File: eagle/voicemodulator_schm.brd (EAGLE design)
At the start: 109 x 84 mm, 36 parts, among them T1 2N5089, T2 2N5089, T3 2N5089, T4 2N5089

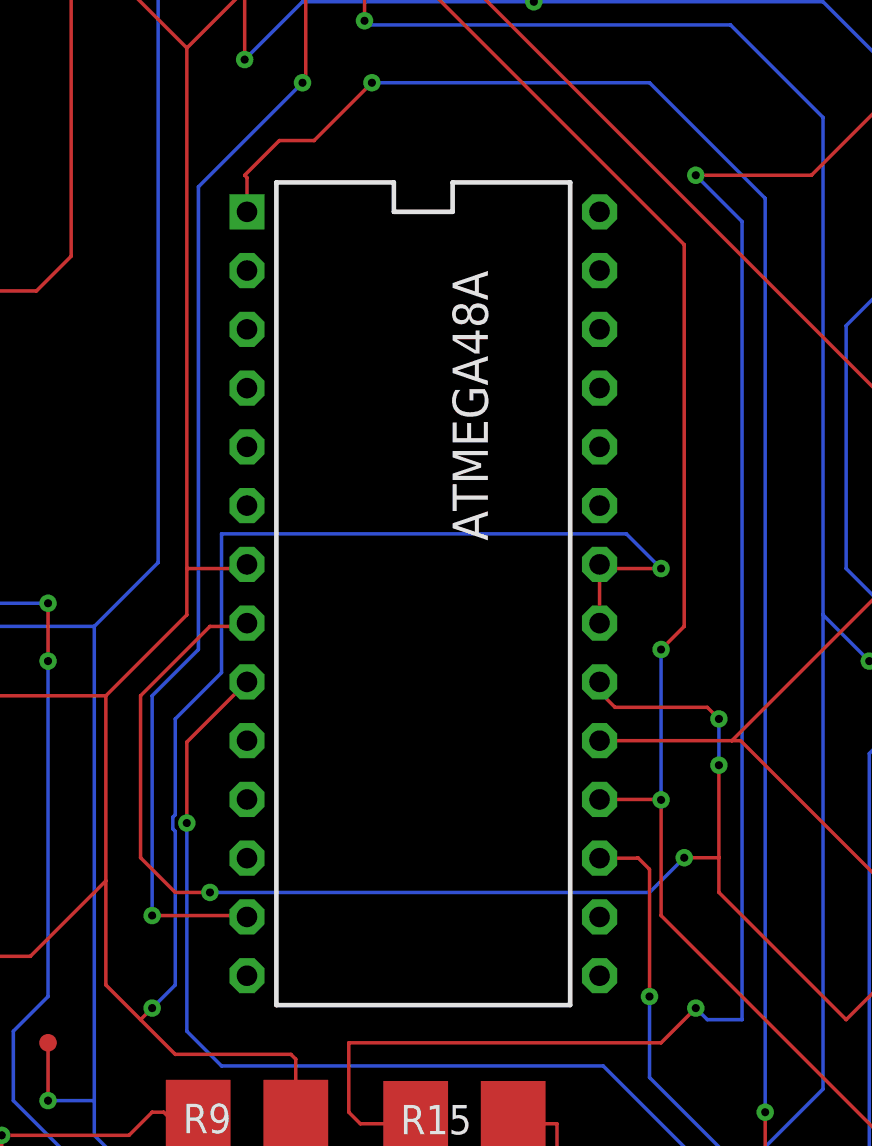
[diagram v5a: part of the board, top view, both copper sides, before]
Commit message: Updated with new model that is adjusted to correct Atmega48A dimensions.
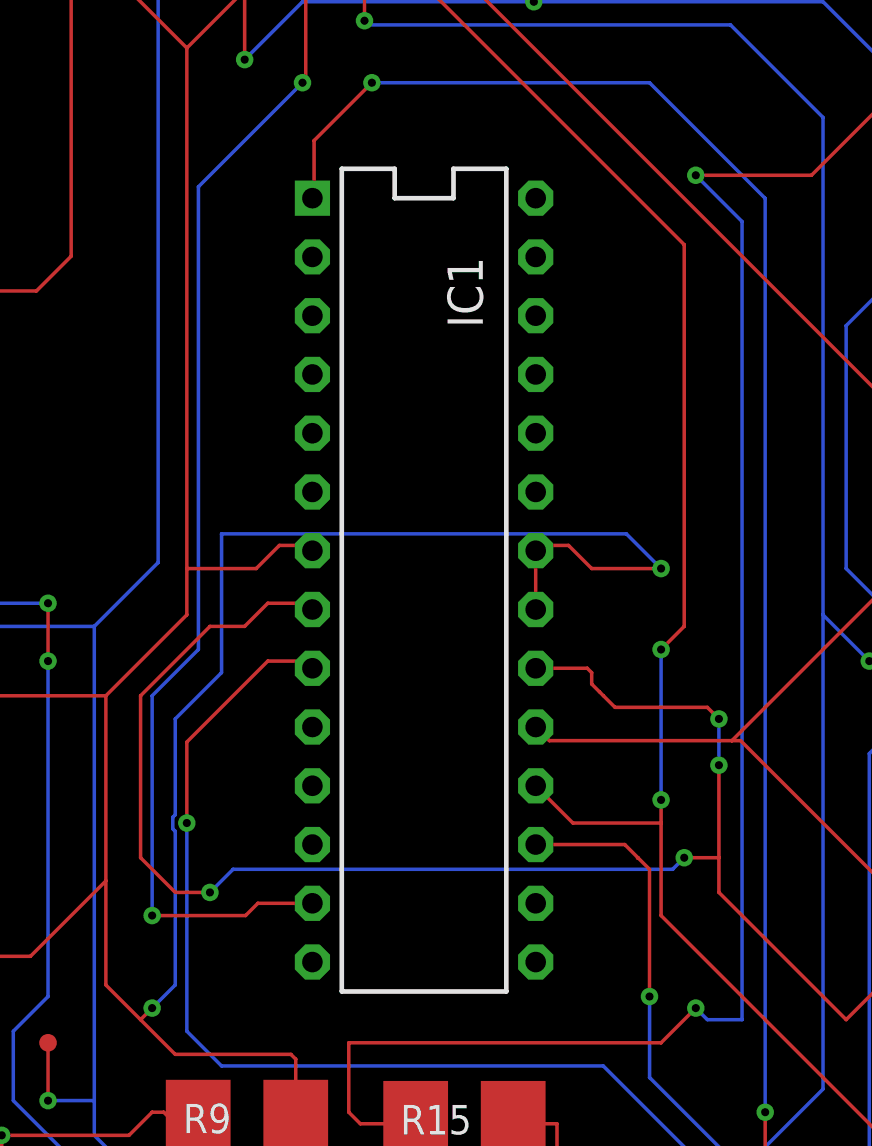
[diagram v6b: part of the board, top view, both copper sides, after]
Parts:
- removed ATMEGA48A: uC, ece411_fixes:DIL28
- added IC1: (no value), voicemod_parts:DIL28
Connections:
- net 0: now also IC1.21, IC1.22, IC1.7; no longer ATMEGA48A.21, ATMEGA48A.22, ATMEGA48A.7
- net N$16: now also IC1.17; no longer ATMEGA48A.17
- net N$17: now also IC1.19; no longer ATMEGA48A.19
- net N$19: now also IC1.13; no longer ATMEGA48A.13
- net N$2: now also IC1.18; no longer ATMEGA48A.18
- net N$20: now also IC1.9; no longer ATMEGA48A.9
- net N$21: now also IC1.20, IC1.8; no longer ATMEGA48A.20, ATMEGA48A.8
- net N$22: now also IC1.1; no longer ATMEGA48A.1
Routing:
- net 0: track 397.4 -> 403.9 mm
- net N$21: track 110.6 -> 116.9 mm
- net N$2: track 78.1 -> 81.5 mm
- net N$20: track 107.1 -> 110.4 mm
- net N$19: track 50.0 -> 53.0 mm
- net N$16: track 142.9 -> 145.9 mm
- net N$17: track 86.8 -> 89.8 mm
- net N$22: track 97.9 -> 95.2 mm

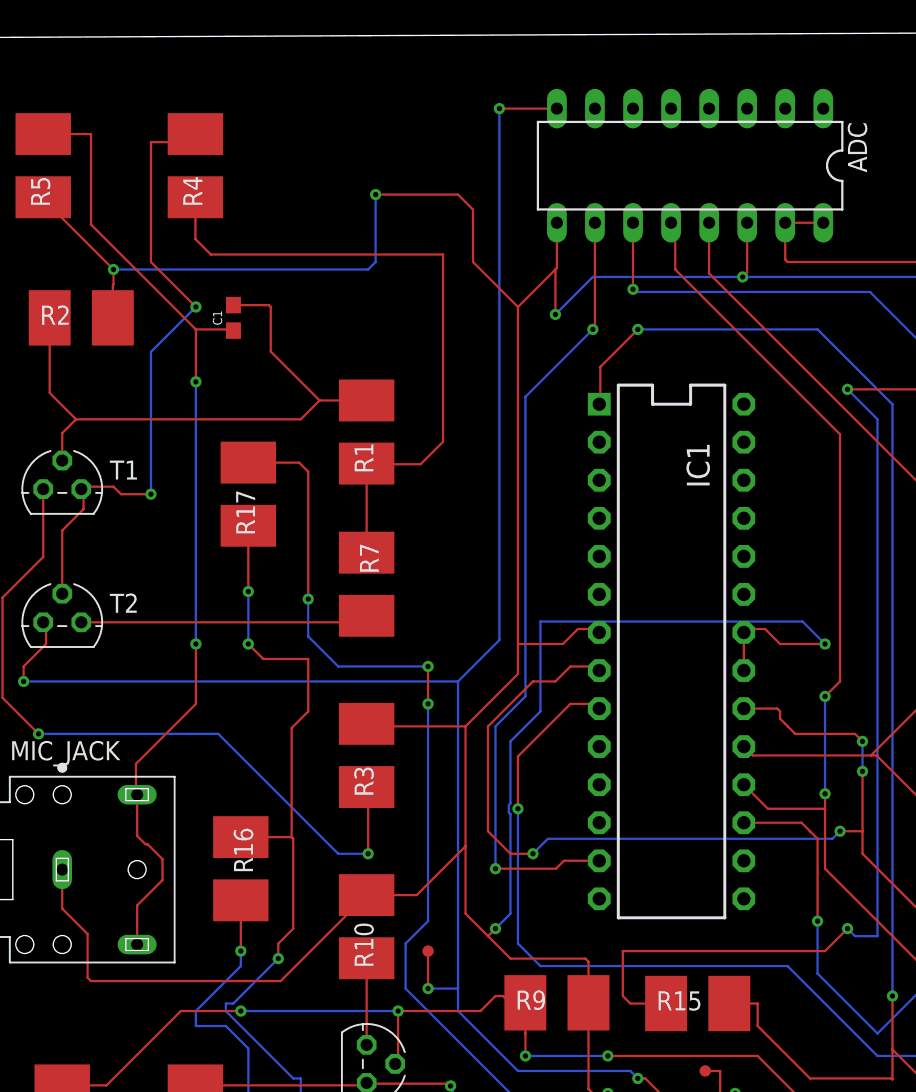
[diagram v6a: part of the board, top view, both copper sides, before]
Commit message: Segmented input with 0 ohm resistors for w/ amp vs. not
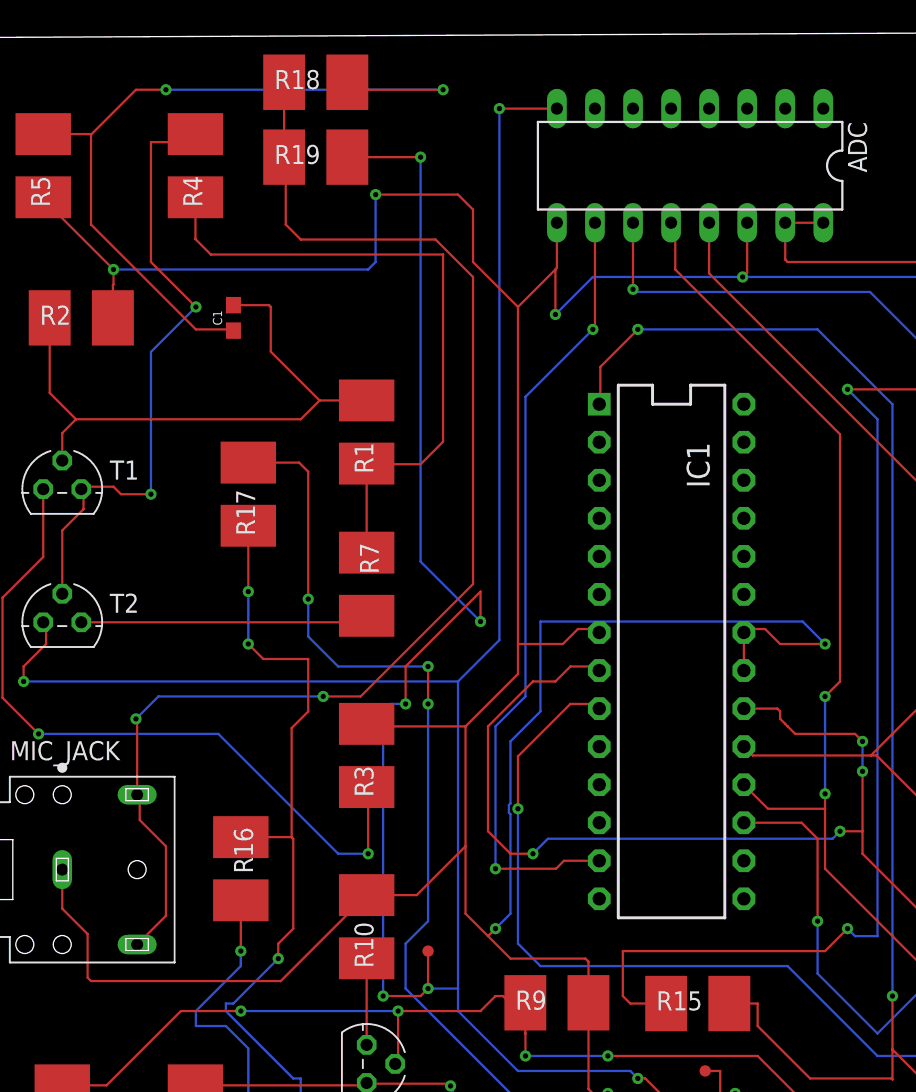
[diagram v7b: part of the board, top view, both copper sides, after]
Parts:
- added R18, R19: (no value), resistor-shunt:SMS-WAV
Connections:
- new net N$24: MIC_JACK.2, MIC_JACK.3, R18.2, R19.2
- net N$1: now also R18.1; no longer MIC_JACK.2, MIC_JACK.3
- net N$5: now also R19.1
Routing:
- net N$24: track 0.00 -> 86.9 mm, vias 0 -> 2
- net N$5: track 147.8 -> 220.8 mm, vias 6 -> 10
- net N$1: track 66.3 -> 53.0 mm
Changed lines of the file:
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@@
 <attribute name="VALUE" x="42.833" y="56.47" size="1.524" layer="27" rot="R270"/>
+</element>
+<element name="R18" library="resistor-shunt" library_urn="urn:adsk.eagle:library:346" package="SMS-WAV" package3d_urn="urn:adsk.eagle:package:25223/1" value="" x="22" y="80.5">
+<attribute name="MF" value="" x="22" y="80.5" size="1.778" layer="27" display="off"/>
+<attribute name="MPN" value="" x="22" y="80.5" size="1.778" layer="27" display="off"/>
+<attribute name="NAME" x="19.2314" y="80.0428" size="1.27" layer="25"/>
+<attribute name="OC_FARNELL" value="unknown" x="22" y="80.5" size="1.778" layer="27" display="off"/>
+<attribute name="OC_NEWARK" value="unknown" x="22" y="80.5" size="1.778" layer="27" display="off"/>
+<attribute name="VALUE" x="18.952" y="77.6044" size="1.27" layer="27"/>
+</element>
+<element name="R19" library="resistor-shunt" library_urn="urn:adsk.eagle:library:346" package="SMS-WAV" package3d_urn="urn:adsk.eagle:package:25223/1" value="" x="22" y="75.5">
+<attribute name="MF" value="" x="22" y="75.5" size="1.778" layer="27" display="off"/>
+<attribute name="MPN" value="" x="22" y="75.5" size="1.778" layer="27" display="off"/>
+<attribute name="NAME" x="19.2314" y="75.0428" size="1.27" layer="25"/>
+<attribute name="OC_FARNELL" value="unknown" x="22" y="75.5" size="1.778" layer="27" display="off"/>
+<attribute name="OC_NEWARK" value="unknown" x="22" y="75.5" size="1.778" layer="27" display="off"/>
+<attribute name="VALUE" x="18.952" y="72.6044" size="1.27" layer="27"/>
 </element>
 </elements>
@@
 </signal>
 <signal name="N$1">
-<contactref element="MIC_JACK" pad="2"/>
-<contactref element="MIC_JACK" pad="3"/>
 <contactref element="C1" pad="1"/>
 <contactref element="R5" pad="1"/>
-<wire x1="10.08" y1="22.94" x2="10.08" y2="25.5468625" width="0.1524" layer="1"/>
-<wire x1="10.08" y1="25.5468625" x2="11.7722" y2="27.2390625" width="0.1524" layer="1"/>
-<wire x1="10.08" y1="32.5" x2="10.08" y2="30.1922" width="0.1524" layer="1"/>
-<wire x1="10.08" y1="32.5" x2="10.08" y2="32.94" width="0.1524" layer="1"/>
-<wire x1="11.7722" y1="28.6409375" x2="11.7722" y2="27.2390625" width="0.1524" layer="1"/>
 <wire x1="16.51" y1="63.92" x2="16.43" y2="64" width="0.1524" layer="1"/>
 <wire x1="16.43" y1="64" x2="14" y2="64" width="0.1524" layer="1"/>
@@
 <wire x1="7" y1="77" x2="6.9618" y2="77.0382" width="0.1524" layer="1"/>
 <wire x1="6.9618" y1="77.0382" x2="3.81" y2="77.0382" width="0.1524" layer="1"/>
-<wire x1="14" y1="64" x2="14" y2="60.5" width="0.1524" layer="1"/>
-<via x="14" y="60.5" extent="1-16" drill="0.35"/>
-<wire x1="14" y1="60.5" x2="14" y2="43" width="0.1524" layer="16"/>
-<via x="14" y="43" extent="1-16" drill="0.35"/>
-<wire x1="14" y1="43" x2="14" y2="39" width="0.1524" layer="1"/>
-<wire x1="14" y1="39" x2="10" y2="35" width="0.1524" layer="1"/>
-<wire x1="10" y1="35" x2="10" y2="32.58" width="0.1524" layer="1"/>
-<wire x1="10" y1="32.58" x2="10.08" y2="32.5" width="0.1524" layer="1"/>
-<wire x1="10.08" y1="30.1922" x2="10.64" y2="29.6322" width="0.1524" layer="1"/>
-<wire x1="10.64" y1="29.6322" x2="10.7809375" y2="29.6322" width="0.1524" layer="1"/>
-<wire x1="10.7809375" y1="29.6322" x2="11.7722" y2="28.6409375" width="0.1524" layer="1"/>
+<contactref element="R18" pad="1"/>
+<wire x1="7" y1="77" x2="10" y2="80" width="0.1524" layer="1"/>
+<wire x1="10" y1="80" x2="12" y2="80" width="0.1524" layer="1"/>
+<via x="12" y="80" extent="1-16" drill="0.35"/>
+<wire x1="12" y1="80" x2="30.5" y2="80" width="0.1524" layer="16"/>
+<via x="30.5" y="80" extent="1-16" drill="0.35"/>
+<wire x1="30.5" y1="80" x2="24.6082" y2="80" width="0.1524" layer="1"/>
+<wire x1="24.6082" y1="80" x2="24.1082" y2="80.5" width="0.1524" layer="1"/>
 </signal>
 <signal name="N$3">
@@
 <via x="29.5" y="20" extent="1-16" drill="0.35"/>
 <wire x1="29.5" y1="20" x2="29.5" y2="22.5" width="0.1524" layer="1"/>
+<contactref element="R19" pad="1"/>
+<wire x1="29.5" y1="20" x2="29" y2="19.5" width="0.1524" layer="1"/>
+<wire x1="29" y1="19.5" x2="26.5" y2="19.5" width="0.1524" layer="1"/>
+<via x="26.5" y="19.5" extent="1-16" drill="0.35"/>
+<wire x1="26.5" y1="19.5" x2="26.5" y2="38.5" width="0.1524" layer="16"/>
+<wire x1="26.5" y1="38.5" x2="27" y2="39" width="0.1524" layer="16"/>
+<wire x1="27" y1="39" x2="28" y2="39" width="0.1524" layer="16"/>
+<via x="28" y="39" extent="1-16" drill="0.35"/>
+<wire x1="28" y1="39" x2="28" y2="41.5" width="0.1524" layer="1"/>
+<wire x1="28" y1="41.5" x2="33" y2="46.5" width="0.1524" layer="1"/>
+<wire x1="33" y1="46.5" x2="33" y2="44.5" width="0.1524" layer="1"/>
+<via x="33" y="44.5" extent="1-16" drill="0.35"/>
+<wire x1="33" y1="44.5" x2="29" y2="48.5" width="0.1524" layer="16"/>
+<wire x1="29" y1="48.5" x2="29" y2="75.5" width="0.1524" layer="16"/>
+<via x="29" y="75.5" extent="1-16" drill="0.35"/>
+<wire x1="29" y1="75.5" x2="24.1082" y2="75.5" width="0.1524" layer="1"/>
 </signal>
 <signal name="N$6">
@@
 <wire x1="73.5" y1="10.5" x2="56" y2="28" width="0.1524" layer="1"/>
 <wire x1="56" y1="28" x2="56" y2="32" width="0.1524" layer="1"/>
-<wire x1="56" y1="32" x2="56" y2="33" width="0.1524" layer="1"/>
-<wire x1="56" y1="33" x2="55.98" y2="33.02" width="0.1524" layer="1"/>
 <wire x1="45.72" y1="71.12" x2="46" y2="70.84" width="0.1524" layer="1"/>
 <wire x1="46" y1="70.84" x2="46" y2="68" width="0.1524" layer="1"/>
@@
 <wire x1="50.58" y1="33.61" x2="52.19" y2="32" width="0.1524" layer="1"/>
 <wire x1="52.19" y1="32" x2="56" y2="32" width="0.1524" layer="1"/>
+<wire x1="56" y1="33" x2="56" y2="32" width="0.1524" layer="1"/>
 </signal>
 <signal name="N$16">
@@
 <via x="55.5" y="24.5" extent="1-16" drill="0.35"/>
 <wire x1="55.5" y1="24.5" x2="55.5" y2="30" width="0.1524" layer="1"/>
-<wire x1="55.5" y1="30" x2="55" y2="30.5" width="0.1524" layer="1"/>
-<wire x1="55" y1="30.5" x2="54.98" y2="30.48" width="0.1524" layer="1"/>
 <via x="75.5" y="3" extent="1-16" drill="0.35"/>
 <wire x1="75.5" y1="3" x2="71" y2="3" width="0.1524" layer="1"/>
 <contactref element="IC1" pad="17"/>
-<wire x1="55" y1="30.5" x2="54.43" y2="31.07" width="0.1524" layer="1"/>
+<wire x1="55.5" y1="30" x2="54.43" y2="31.07" width="0.1524" layer="1"/>
 <wire x1="54.43" y1="31.07" x2="50.58" y2="31.07" width="0.1524" layer="1"/>
 </signal>
@@
 <wire x1="50" y1="10" x2="52.49" y2="10" width="0.1524" layer="1"/>
 </signal>
+<signal name="N$24">
+<contactref element="MIC_JACK" pad="2"/>
+<contactref element="MIC_JACK" pad="3"/>
+<contactref element="R18" pad="2"/>
+<contactref element="R19" pad="2"/>
+<wire x1="10.25" y1="31.25" x2="12" y2="29.5" width="0.1524" layer="1"/>
+<wire x1="12" y1="29.5" x2="12" y2="24.86" width="0.1524" layer="1"/>
+<wire x1="12" y1="24.86" x2="10.08" y2="22.94" width="0.1524" layer="1"/>
+<wire x1="19.8918" y1="75.5" x2="19.8918" y2="80.5" width="0.1524" layer="1"/>
+<wire x1="19.8918" y1="75.5" x2="20" y2="75.3918" width="0.1524" layer="1"/>
+<wire x1="20" y1="75.3918" x2="20" y2="71" width="0.1524" layer="1"/>
+<wire x1="20" y1="71" x2="21" y2="70" width="0.1524" layer="1"/>
+<wire x1="21" y1="70" x2="30" y2="70" width="0.1524" layer="1"/>
+<wire x1="30" y1="70" x2="32.5" y2="67.5" width="0.1524" layer="1"/>
+<wire x1="32.5" y1="67.5" x2="32.5" y2="47" width="0.1524" layer="1"/>
+<wire x1="32.5" y1="47" x2="25" y2="39.5" width="0.1524" layer="1"/>
+<wire x1="25" y1="39.5" x2="22.5" y2="39.5" width="0.1524" layer="1"/>
+<via x="22.5" y="39.5" extent="1-16" drill="0.35"/>
+<wire x1="22.5" y1="39.5" x2="11.5" y2="39.5" width="0.1524" layer="16"/>
+<wire x1="11.5" y1="39.5" x2="10" y2="38" width="0.1524" layer="16"/>
+<via x="10" y="38" extent="1-16" drill="0.35"/>
+<wire x1="10" y1="38" x2="10.08" y2="37.92" width="0.1524" layer="1"/>
+<wire x1="10.08" y1="37.92" x2="10.08" y2="32.94" width="0.1524" layer="1"/>
+<wire x1="10.08" y1="32.94" x2="10.25" y2="32.77" width="0.1524" layer="1"/>
+<wire x1="10.25" y1="32.77" x2="10.25" y2="31.25" width="0.1524" layer="1"/>
+</signal>
 </signals>

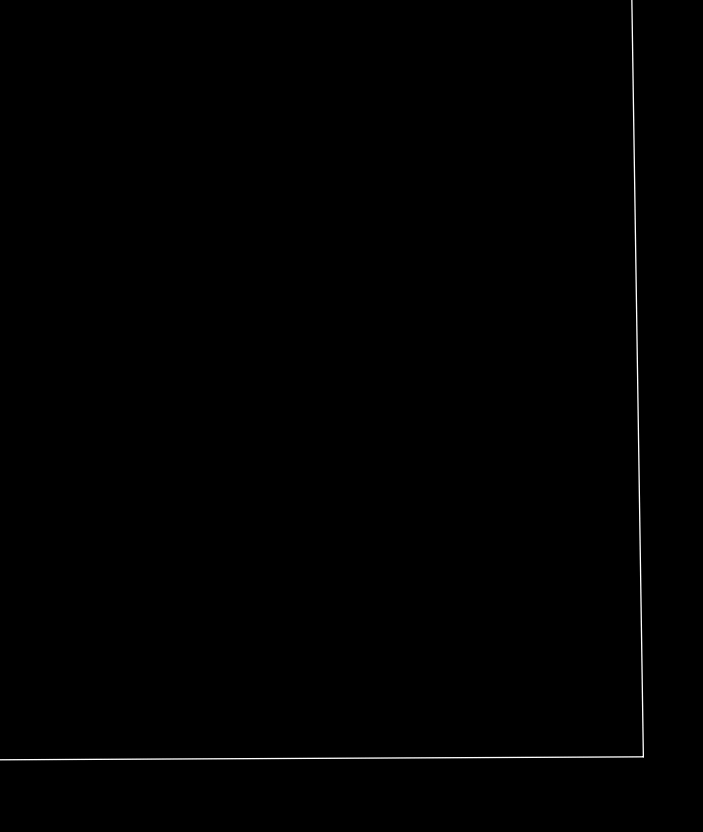
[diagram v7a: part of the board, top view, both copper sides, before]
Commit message: USB 3.0 Type A Port Added, pinout TBD
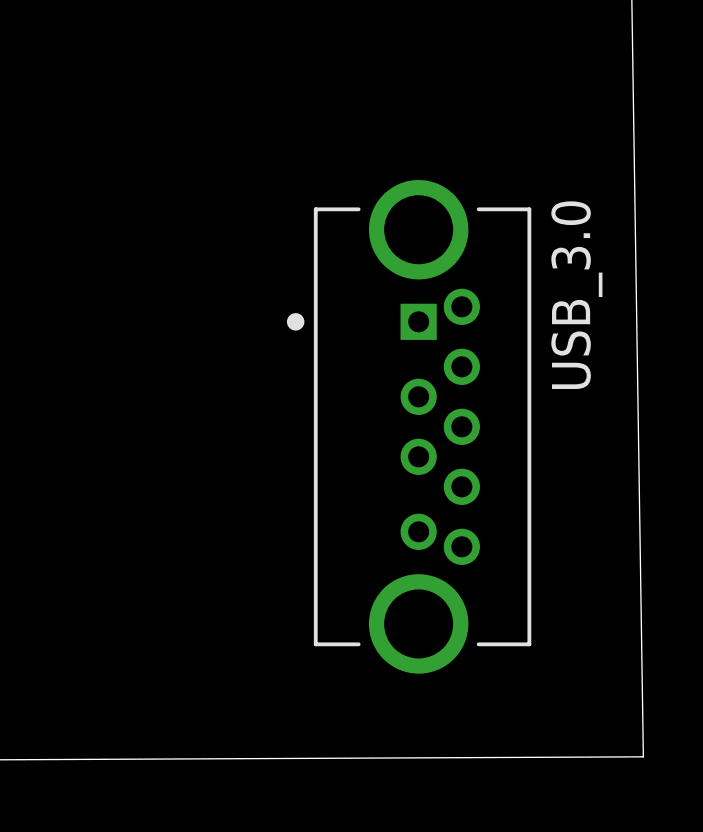
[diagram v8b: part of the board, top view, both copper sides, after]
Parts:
- added USB_3.0: 10117836-002LF, USB_SMT_3:AMPHENOL_10117836-002LF
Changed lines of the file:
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@@
 <attribute name="VALUE" x="18.952" y="72.6044" size="1.27" layer="27"/>
+</element>
+<element name="USB_3.0" library="USB_SMT_3" package="AMPHENOL_10117836-002LF" value="10117836-002LF" x="101.5" y="11.5" rot="R270">
+<attribute name="AVAILABILITY" value="Unavailable" x="101.5" y="11.5" size="1.778" layer="27" rot="R270" display="off"/>
+<attribute name="DESCRIPTION" value=" Usb, 3.0 Type A, Receptacle, SMT " x="101.5" y="11.5" size="1.778" layer="27" rot="R270" display="off"/>
+<attribute name="MF" value="Amphenol FCI" x="101.5" y="11.5" size="1.778" layer="27" rot="R270" display="off"/>
+<attribute name="MP" value="10117836-002LF" x="101.5" y="11.5" size="1.778" layer="27" rot="R270" display="off"/>
+<attribute name="NAME" x="105.945" y="19.12" size="1.27" layer="25" rot="R270"/>
+<attribute name="PACKAGE" value="None" x="101.5" y="11.5" size="1.778" layer="27" rot="R270" display="off"/>
+<attribute name="PRICE" value="None" x="101.5" y="11.5" size="1.778" layer="27" rot="R270" display="off"/>
+<attribute name="VALUE" x="95.785" y="19.12" size="1.27" layer="27" rot="R270"/>
 </element>
 </elements>
